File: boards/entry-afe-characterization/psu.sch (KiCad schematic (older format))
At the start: 0 parts

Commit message: Continued work on AFE characterization board
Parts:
- added C? (x2): 0.1 uF, symbol device:C
- added C? (x2): 300 pF, symbol device:C
- added C? (x2): 4.7 uF, symbol device:C
- added R? (x3): 1K 1%, symbol device:R
- added R?: 1.33K 1%, symbol device:R
- added U?: MCP1501T-10E/RW, symbol analog-azonenberg:MCP1501_DFN
- added U?: MCP1501T-40E/SN, symbol analog-azonenberg:MCP1501_SOIC
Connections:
- net labels added: 0V5_REF, 1V0_REF, 5V0_N, 5V0_P, GND, N0V5_REF, N0V9_REF
- wire segments 0 -> 35
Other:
- note added: "+1.024V reference\nDivide by 2 to get a 512 mV reference"
- note added: "+4.096V voltage reference\nShifted down to -5V\nOUT pin is thus -0.904V\nDivider output is -516 mV"

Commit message: Continued work on AFE characterization board. Still have to do power supply.
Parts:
- removed C? (x2): 0.1 uF, symbol device:C
- removed C? (x2): 300 pF, symbol device:C
- removed C? (x2): 4.7 uF, symbol device:C
- removed R? (x3): 1K 1%, symbol device:R
- removed R?: 1.33K 1%, symbol device:R
- removed U?: MCP1501T-10E/RW, symbol analog-azonenberg:MCP1501_DFN
- removed U?: MCP1501T-40E/SN, symbol analog-azonenberg:MCP1501_SOIC
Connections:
- net labels removed: 1V0_REF, 5V0_N, 5V0_P, GND, N0V9_REF
- wire segments 35 -> 0
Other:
- note added: "13K, 1.5K -> 0.517V for +/- 5V rails"
- note added: "Generate +/- 0.5V ref's with voltage dividers and bigger caps"
- note added: "LT3093"
- note removed: "+1.024V reference\nDivide by 2 to get a 512 mV reference"

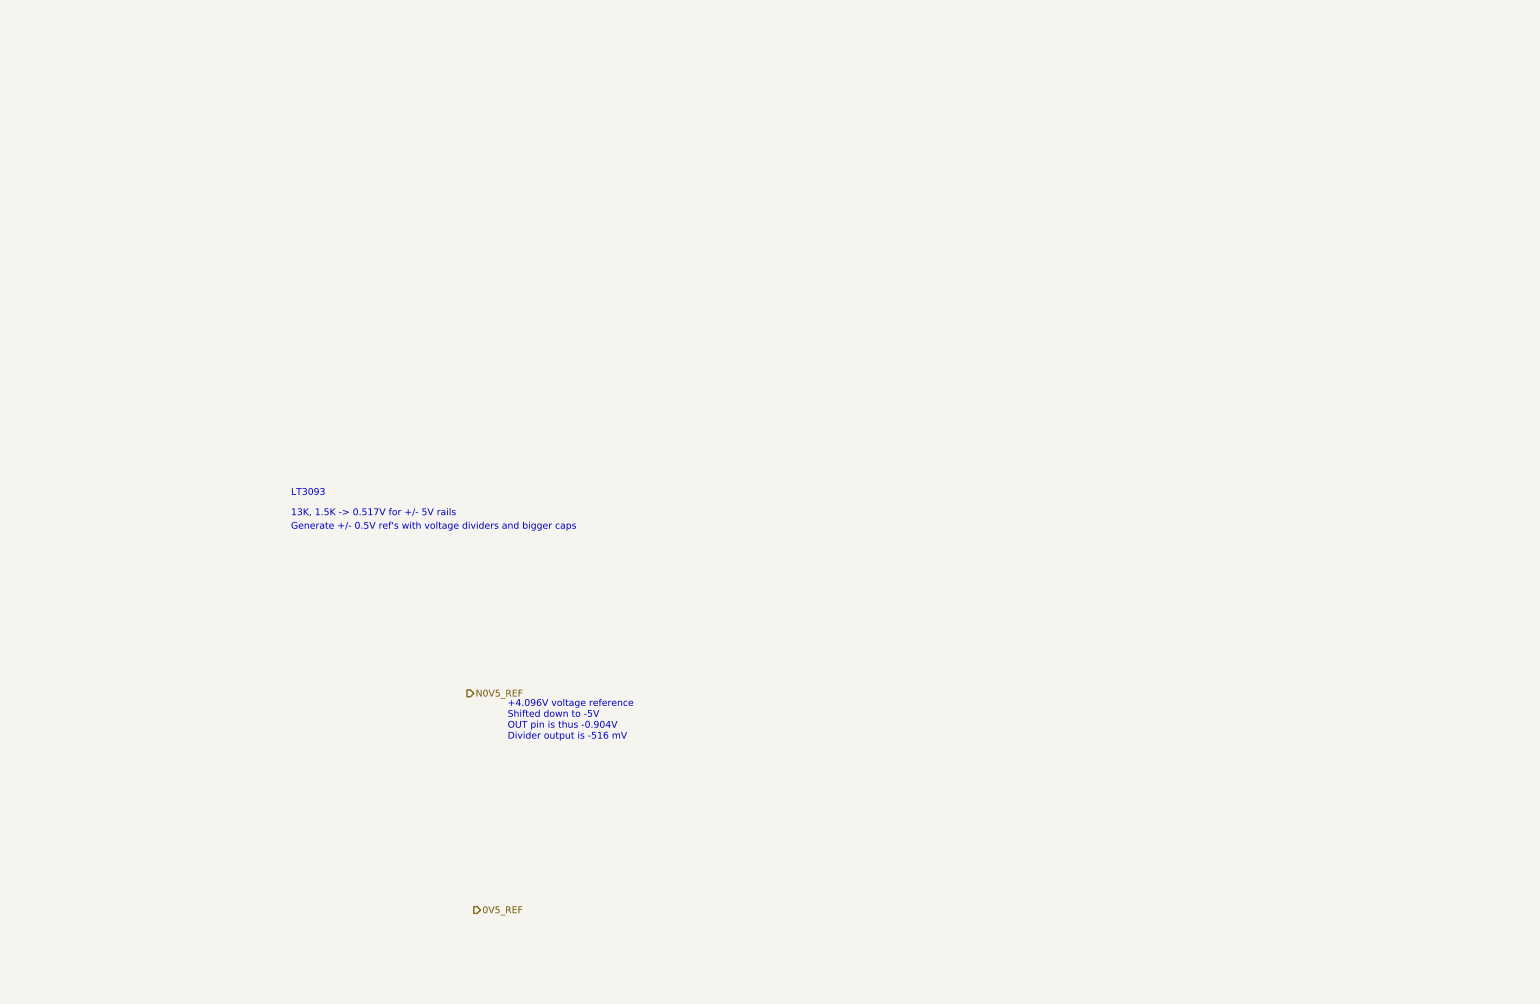
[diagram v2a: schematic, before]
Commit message: Updated entry-afe-characterization with progress on power supply
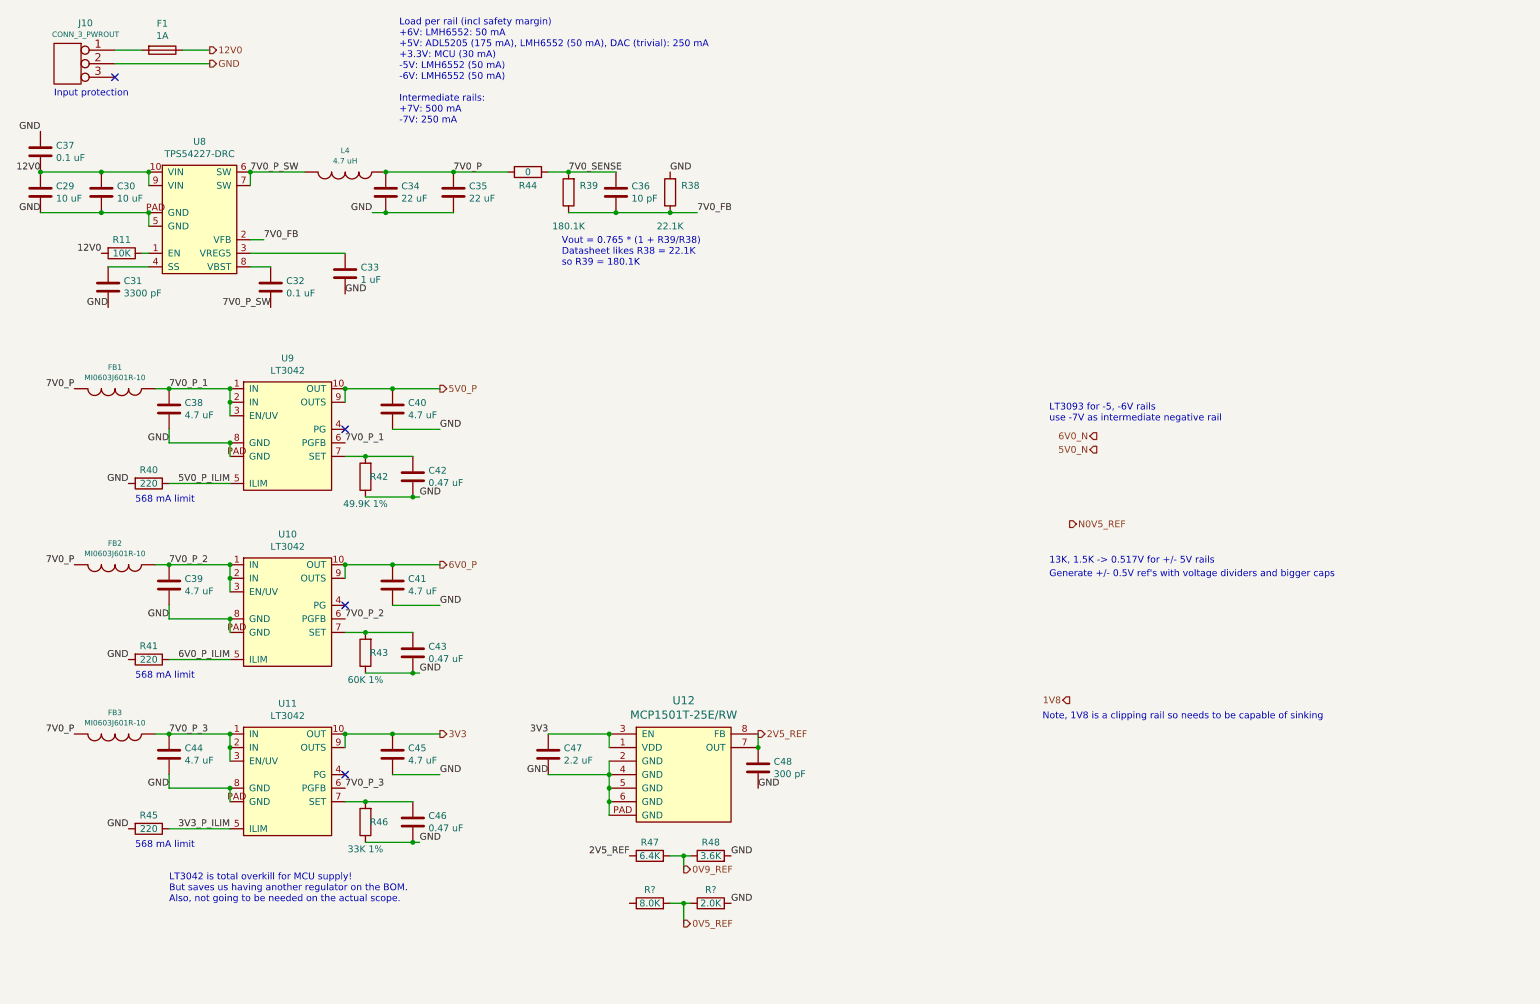
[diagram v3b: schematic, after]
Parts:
- added C29, C30: 10 uF, symbol device:C
- added C31: 3300 pF, symbol device:C
- added C32, C37: 0.1 uF, symbol device:C
- added C33: 1 uF, symbol device:C
- added C34, C35: 22 uF, symbol device:C
- added C36: 10 pF, symbol device:C
- added C38, C39, C40, C41, C44, C45: 4.7 uF, symbol device:C
- added C42, C43, C46: 0.47 uF, symbol device:C
- added C47: 2.2 uF, symbol device:C
- added C48: 300 pF, symbol device:C
- added F1: 1A, symbol device:Fuse
- added FB1, FB2, FB3: MI0603J601R-10, symbol passive-azonenberg:INDUCTOR_PWROUT
- added J10: CONN_3_PWROUT, symbol power-azonenberg:CONN_3_PWROUT
- added L4: 4.7 uH, symbol passive-azonenberg:INDUCTOR_PWROUT
- added R11: 10K, symbol device:R
- added R38: 22.1K, symbol device:R
- added R39: 180.1K, symbol device:R
- added R40, R41, R45: 220, symbol device:R
- added R42: 49.9K 1%, symbol device:R
- added R43: 60K 1%, symbol device:R
- added R44: 0, symbol device:R
- added R46: 33K 1%, symbol device:R
- added R47: 6.4K, symbol device:R
- added R48: 3.6K, symbol device:R
- added R?: 8.0K, symbol device:R
- added R?: 2.0K, symbol device:R
- added U10, U11, U9: LT3042, symbol power-azonenberg:LT3042
- added U12: MCP1501T-25E/RW, symbol analog-azonenberg:MCP1501_DFN
- added U8: TPS54227-DRC, symbol power-azonenberg:TPS54227-DRC
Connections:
- net 0V5_REF: now also R?.1, R?.2
- new net: R11.1, U8.1 (EN)
- new net: C33.1, U8.3 (VREG5)
- new net: C31.1, U8.4 (SS)
- new net: C32.1, U8.8 (VBST)
- new net: C42.1, R42.2, U9.7 (SET)
- new net: C43.1, R43.2, U10.7 (SET)
- new net: C46.1, R46.2, U11.7 (SET)
- new net: F1.2, J10.1 (P1)
- new net 0V9_REF: R47.2, R48.1
- new net 12V0: C29.1, C30.1, C37.2, F1.1, R11.2, U8.10 (VIN), U8.9 (VIN)
- new net 2V5_REF: C48.1, R47.1, U12.7 (OUT), U12.8 (FB)
- new net 3V3: C45.1, C47.1, U11.10 (OUT), U11.9 (OUTS), U12.1 (VDD), U12.3 (EN)
- new net 3V3_P_ILIM: R45.1, U11.5 (ILIM)
- new net 5V0_P: C40.1, U9.10 (OUT), U9.9 (OUTS)
- new net 5V0_P_ILIM: R40.1, U9.5 (ILIM)
- new net 6V0_P: C41.1, U10.10 (OUT), U10.9 (OUTS)
- new net 6V0_P_ILIM: R41.1, U10.5 (ILIM)
- new net 7V0_FB: C36.1, R38.1, R39.1, U8.2 (VFB)
- new net 7V0_P: C34.1, C35.1, FB1.2, FB2.2, FB3.2, L4.1, R44.1
- new net 7V0_P_1: C38.1, FB1.1, U9.1 (IN), U9.2 (IN), U9.3 (EN/UV), U9.6 (PGFB)
- new net 7V0_P_2: C39.1, FB2.1, U10.1 (IN), U10.2 (IN), U10.3 (EN/UV), U10.6 (PGFB)
- new net 7V0_P_3: C44.1, FB3.1, U11.1 (IN), U11.2 (IN), U11.3 (EN/UV), U11.6 (PGFB)
- new net 7V0_P_SW: C32.2, L4.2, U8.6 (SW), U8.7 (SW)
- new net 7V0_SENSE: C36.2, R39.2, R44.2
- new net GND: C29.2, C30.2, C31.2, C33.2, C34.2, C35.2, C37.1, C38.2, C39.2, C40.2, C41.2, C42.2, C43.2, C44.2, C45.2, C46.2, C47.2, C48.2, J10.2 (PM), R38.2, R40.2, R41.2, R42.1, R43.1, R45.2, R46.1, R48.2, R?.2, U10.8 (GND), U10.PAD (GND), U11.8 (GND), U11.PAD (GND), U12.2 (GND), U12.4 (GND), U12.5 (GND), U12.6 (GND), U12.PAD (GND), U8.5 (GND), U8.PAD (GND), U9.8 (GND), U9.PAD (GND)
- no-connect marks 0 -> 4
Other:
- note added: "568 mA limit"
- note added: "Input protection"
- note added: "LT3042 is total overkill for MCU supply!\nBut saves us having another regulator on the BOM.\nAlso, not going to be needed on the actual scope."
- note added: "LT3093 for -5, -6V rails\nuse -7V as intermediate negative rail"
- note added: "Load per rail (incl safety margin)\n+6V: LMH6552: 50 mA\n+5V: ADL5205 (175 mA), LMH6552 (50 mA), DAC (trivial): 250 mA\n+3.3V: MCU (30 mA)\n-5V: LMH6552 (50 mA)\n-6V: LMH6552 (50 mA)\n\nIntermediate rails:\n+7V: 500 mA\n-7V: 250 mA"
- note added: "Note, 1V8 is a clipping rail so needs to be capable of sinking"
- note added: "Vout = 0.765 * (1 + R39/R38)\nDatasheet likes R38 = 22.1K\nso R39 = 180.1K"
- note removed: "+4.096V voltage reference\nShifted down to -5V\nOUT pin is thus -0.904V\nDivider output is -516 mV"
- note removed: "LT3093"

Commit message: Final iteration of entry-afe-characterization, ready for schematic review
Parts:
- added C49, C53: 220 uF, symbol device:CP1
- added C50: 47 uF, symbol device:C
- added C51, C52, C55, C56, C57, C58, C61, C62: 4.7 uF, symbol device:C
- added C54: 10 uF, symbol device:C
- added C59, C60: 0.47 uF, symbol device:C
- added C63: 22 pF, symbol device:C
- added C64, C65: 22 uF, symbol device:C
- added FB4, FB5: MI0603J601R-10, symbol passive-azonenberg:INDUCTOR_PWROUT
- added Q2: 2SA2039-TL-E, symbol device:Q_PNP_BCEC
- added R51: 11.5K 1%, symbol device:R
- added R52: 470, symbol device:R
- added R54: 9.0K, symbol device:R
- added R55: 1.0K, symbol device:R
- added R56, R57: 60K 1%, symbol device:R
- added U13, U15: LT3093, symbol power-azonenberg:LT3093
- added U14: PTN78000AAZ, symbol power-azonenberg:PTN78000AAZ
- added U16: LT3042, symbol power-azonenberg:LT3042
- added U17: TL431ACDBZR, symbol analog-azonenberg:TL431A_SOT23_TI_DBZ
- R40: value 220 -> 470
- R41: value 220 -> 4.7K
- R45: value 220 -> 2.7K
- gave numbers to parts that had none: 2
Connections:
- net 12V0: now also C49.1, C50.1, C51.1, C52.1, U14.2 (VIN)
- net 1V8: now also R40.2, R41.1, C64.1, Q2.3 (E), R52.1
- net 2V5_REF: now also R49.1
- net 5V0_N: now also R45.2, C58.1, C65.2, R54.1, U15.10 (OUTS), U15.11 (OUT), U15.12 (OUT), U17.3
- net 5V0_P: now also R40.1, C62.1, U16.10 (OUT), U16.9 (OUTS)
- net 6V0_N: now also C57.1, U13.10 (OUTS), U13.11 (OUT), U13.12 (OUT)
- net 7V0_P_1: now also C61.1, U16.1 (IN), U16.2 (IN), U16.3 (EN/UV), U16.6 (PGFB)
- net GND: now also U10.5 (ILIM), U11.5 (ILIM), U9.5 (ILIM), C49.2, C50.2, C51.2, C52.2, C53.1, C54.2, C55.2, C56.2, C57.2, C58.2, C59.2, C60.2, C61.2, C62.2, C64.2, C65.1, Q2.2 (C), Q2.4 (C), R55.2, R56.2, R57.2, U13.6 (ILIM), U13.9 (GND), U14.5 (GND), U15.6 (ILIM), U15.9 (GND), U16.5 (ILIM), U16.8 (GND), U16.PAD (GND); no longer R40.2, R41.2, R45.2
- net N0V5_REF: now also R54.2, R55.1
- net 5V0_P_SET: now reaches C42.1, R42.2, U9.7 (SET)
- net 5V0_P_SET: now also U16.7 (SET)
- net 3V3_P_ILIM: no longer names the net of R45.1
- net 3V3_P_ILIM: now also R41.2, C63.2, U17.2; no longer U11.5 (ILIM)
- removed net 5V0_P_ILIM: R40.1, U9.5 (ILIM)
- removed net 6V0_P_ILIM: R41.1, U10.5 (ILIM)
- new net: C59.1, R56.1, U13.8 (SET)
- new net: C60.1, R57.1, U15.8 (SET)
- new net: C63.1, Q2.1 (B), R52.2, U17.1
- new net 7V0_ADJ: R51.1, U14.4 (ADJ)
- new net 7V0_N: C53.2, C54.1, FB4.2, FB5.2, R51.2, U14.1 (VOUT)
- new net 7V0_N_1: C55.1, FB4.1, U13.1 (IN), U13.2 (IN), U13.3 (EN/UV), U13.5 (PGFB), U13.PAD (IN)
- new net 7V0_N_2: C56.1, FB5.1, U15.1 (IN), U15.2 (IN), U15.3 (EN/UV), U15.5 (PGFB), U15.PAD (IN)
- no-connect marks 4 -> 9
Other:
- note added: "1V8 is a clipping rail so we need a SINK regulator.\nNot commonly available so we have to build one.\nSee design notes:\nhttps://github.com/electroniceel/io-protection-notes/tree/master/power-shunt"
- note added: "Parallel U9/U16 for increased current"
- note removed: "13K, 1.5K -> 0.517V for +/- 5V rails"
- note removed: "568 mA limit"
- note removed: "Generate +/- 0.5V ref's with voltage dividers and bigger caps"
- note removed: "LT3093 for -5, -6V rails\nuse -7V as intermediate negative rail"
- note removed: "Note, 1V8 is a clipping rail so needs to be capable of sinking"
- moved on the sheet: C32, C33, C36, C39, C41, C43, C44, C45, C46, C47, C48, FB2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

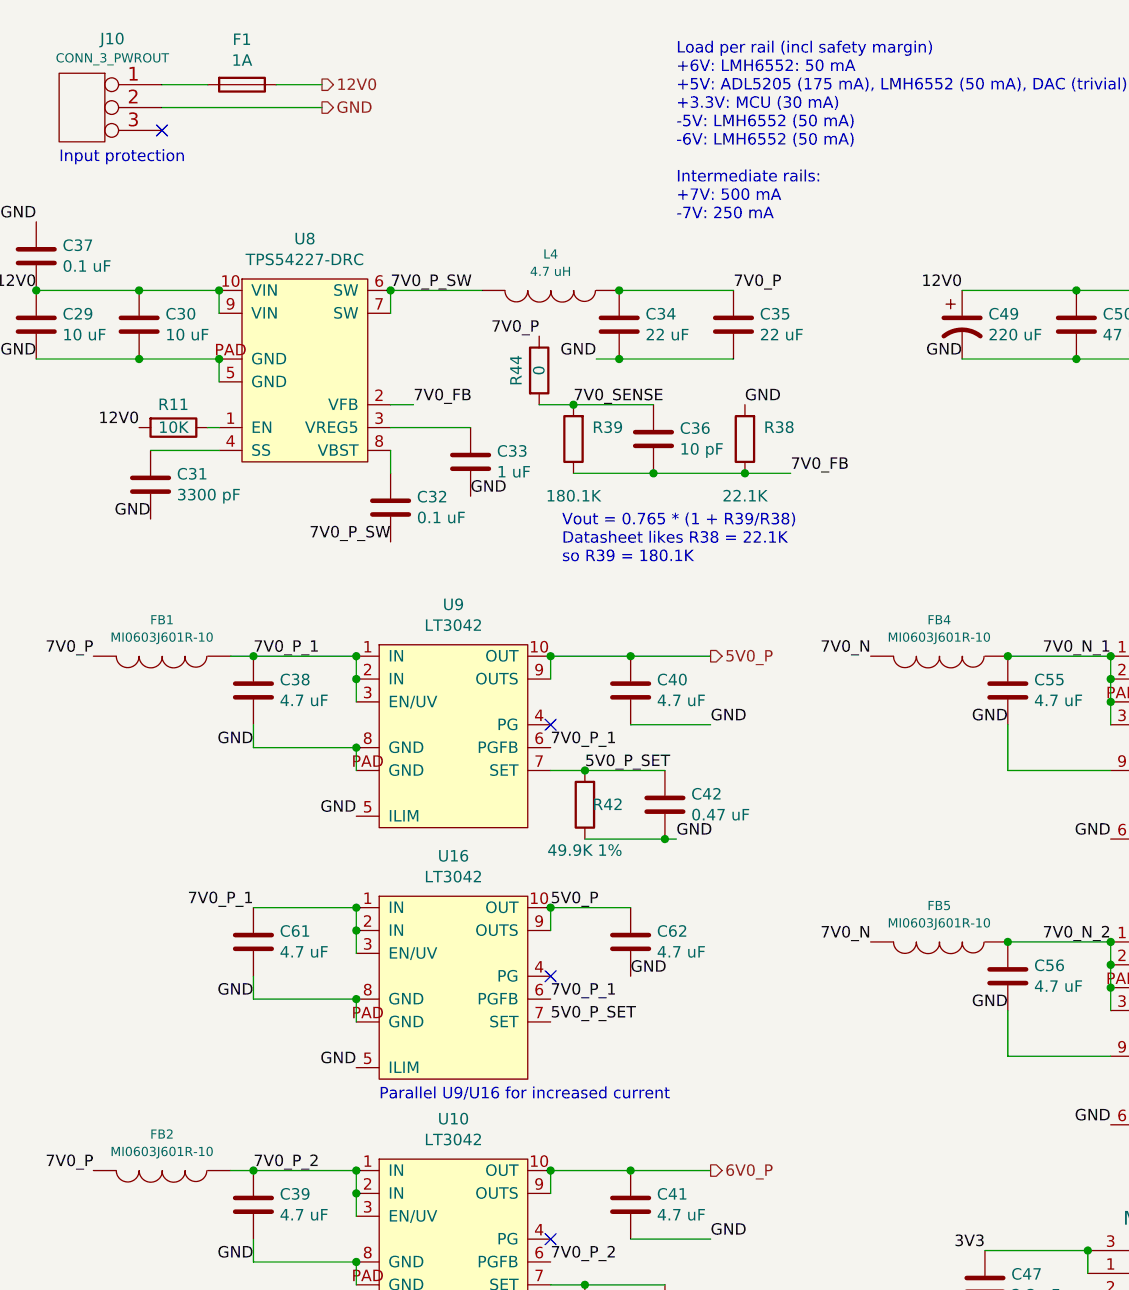
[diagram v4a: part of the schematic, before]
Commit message: Began entry-afe-characterization design review
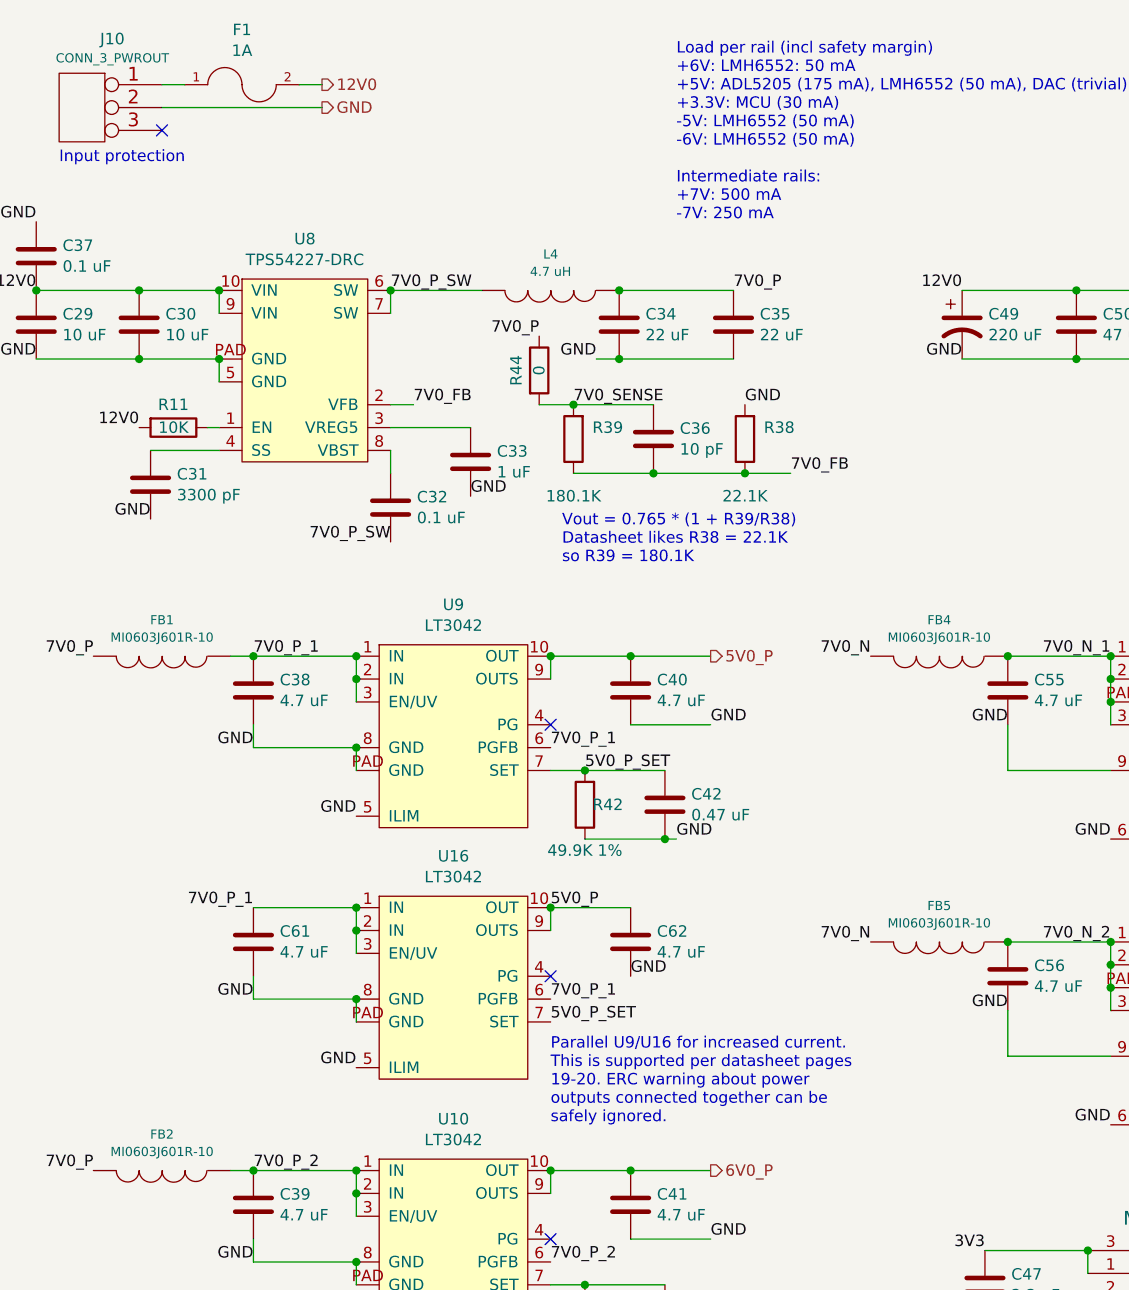
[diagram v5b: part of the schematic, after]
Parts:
- removed F1: 1A, symbol device:Fuse
- added F1: 1A, symbol power-azonenberg:FUSE_PWROUT
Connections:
- net 12V0: now also F1.2
- net at J10.1 (P1): now also F1.1
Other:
- note added: "Parallel U9/U16 for increased current.\nThis is supported per datasheet pages\n19-20. ERC warning about power\noutputs connected together can be\nsafely ignored."
- note removed: "Parallel U9/U16 for increased current"
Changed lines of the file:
@@
 $EndComp
 NoConn ~ 1250 1000
-$Comp
-L device:Fuse F1
-U 1 1 5E811BC3
-P 1600 800
-F 0 "F1" V 1403 800 50  0000 C CNN
-F 1 "1A" V 1494 800 50  0000 C CNN
-F 2 "" V 1530 800 50  0001 C CNN
-F 3 "" H 1600 800 50  0001 C CNN
-	1    1600 800
-	0    1    1    0
-$EndComp
-Wire Wire Line
-	1450 800  1250 800
-Wire Wire Line
-	1750 800  1950 800
 Text HLabel 3650 5550 2    50   Output ~ 0
 6V0_P
@@
 Text Label 3300 4700 0    50   ~ 0
 GND
-Text Notes 2200 5250 0    50   ~ 0
-Parallel U9/U16 for increased current
+Text Notes 2950 5350 0    50   ~ 0
+Parallel U9/U16 for increased current.\nThis is supported per datasheet pages\n19-20. ERC warning about power\noutputs connected together can be\nsafely ignored.
 Text Label 5450 7500 2    50   ~ 0
 5V0_N
@@
 	10200 5150 8600 5150
 Connection ~ 8600 5150
+$Comp
+L power-azonenberg:FUSE_PWROUT F1
+U 1 1 5E9EE5E6
+P 1600 800
+F 0 "F1" H 1600 1040 50  0000 C CNN
+F 1 "1A" H 1600 949 50  0000 C CNN
+F 2 "" H 1600 800 60  0000 C CNN
+F 3 "" H 1600 800 60  0000 C CNN
+	1    1600 800
+	1    0    0    -1
+$EndComp
+Wire Wire Line
+	1250 800  1350 800
+Wire Wire Line
+	1850 800  1950 800
 $EndSCHEMATC
